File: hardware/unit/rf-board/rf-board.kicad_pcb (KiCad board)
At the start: 6 copper layers, 268 x 230 mm, 357 parts, among them J1 83-798 SO-239, J10 83-798 SO-239, J11 XT60PW-M, J12 XT60PW-M, J13 XT30PW-M, J14 Controller header, J2 83-798 SO-239, J3 83-798 SO-239, J4 SMA jack EXP, J5 SMA jack EXP, J6 SMA jack EXP, J7 83-798 SO-239, J8 83-798 SO-239, J9 83-798 SO-239, K101 RTD14012F, K102 RTD14012F, K103 RTD14012F, K104 RTD14012F, K105 RTD14012F, K106 RTD14012F, K107 RTD14012F, K108 RTD14012F, K109 RTD14012F, K110 RTD14012F, K111 RTD14012F, K201 RTD14012F, K202 RTD14012F, K203 RTD14012F, K204 RTD14012F, K205 RTD14012F, K206 RTD14012F, K207 RTD14012F, K208 RTD14012F, K209 RTD14012F, K210 RTD14012F, K211 RTD14012F, K301 RTD14012F, K302 RTD14012F, K303 RTD14012F, K304 RTD14012F, K305 RTD14012F, K306 RTD14012F, K307 RTD14012F, K308 RTD14012F, K309 RTD14012F, K310 RTD14012F, K311 RTD14012F, K401 RTD14012F, K501 RTD14012F, K601 RTD14012F, K701 RTD14012F, Q1 PMV50EPEA, Q101 BSS138BK, Q1011 BC857B, Q1012 IRFL9014, Q1013 BSS138BK, Q102 BSS138BK, Q1021 BC857B, Q1022 IRFL9014, Q1023 BSS138BK, Q103 BSS138BK, Q1031 BC857B, Q1032 IRFL9014, Q1033 BSS138BK, Q104 BSS138BK, Q1041 BC857B, Q1042 IRFL9014, Q1043 BSS138BK, Q105 BSS138BK, Q106 BSS138BK, Q107 BSS138BK, Q108 BSS138BK, Q109 BSS138BK, Q110 BSS138BK, Q111 BSS138BK, Q2 BSS138BK, Q201 BSS138BK, Q202 BSS138BK, Q203 BSS138BK, Q204 BSS138BK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

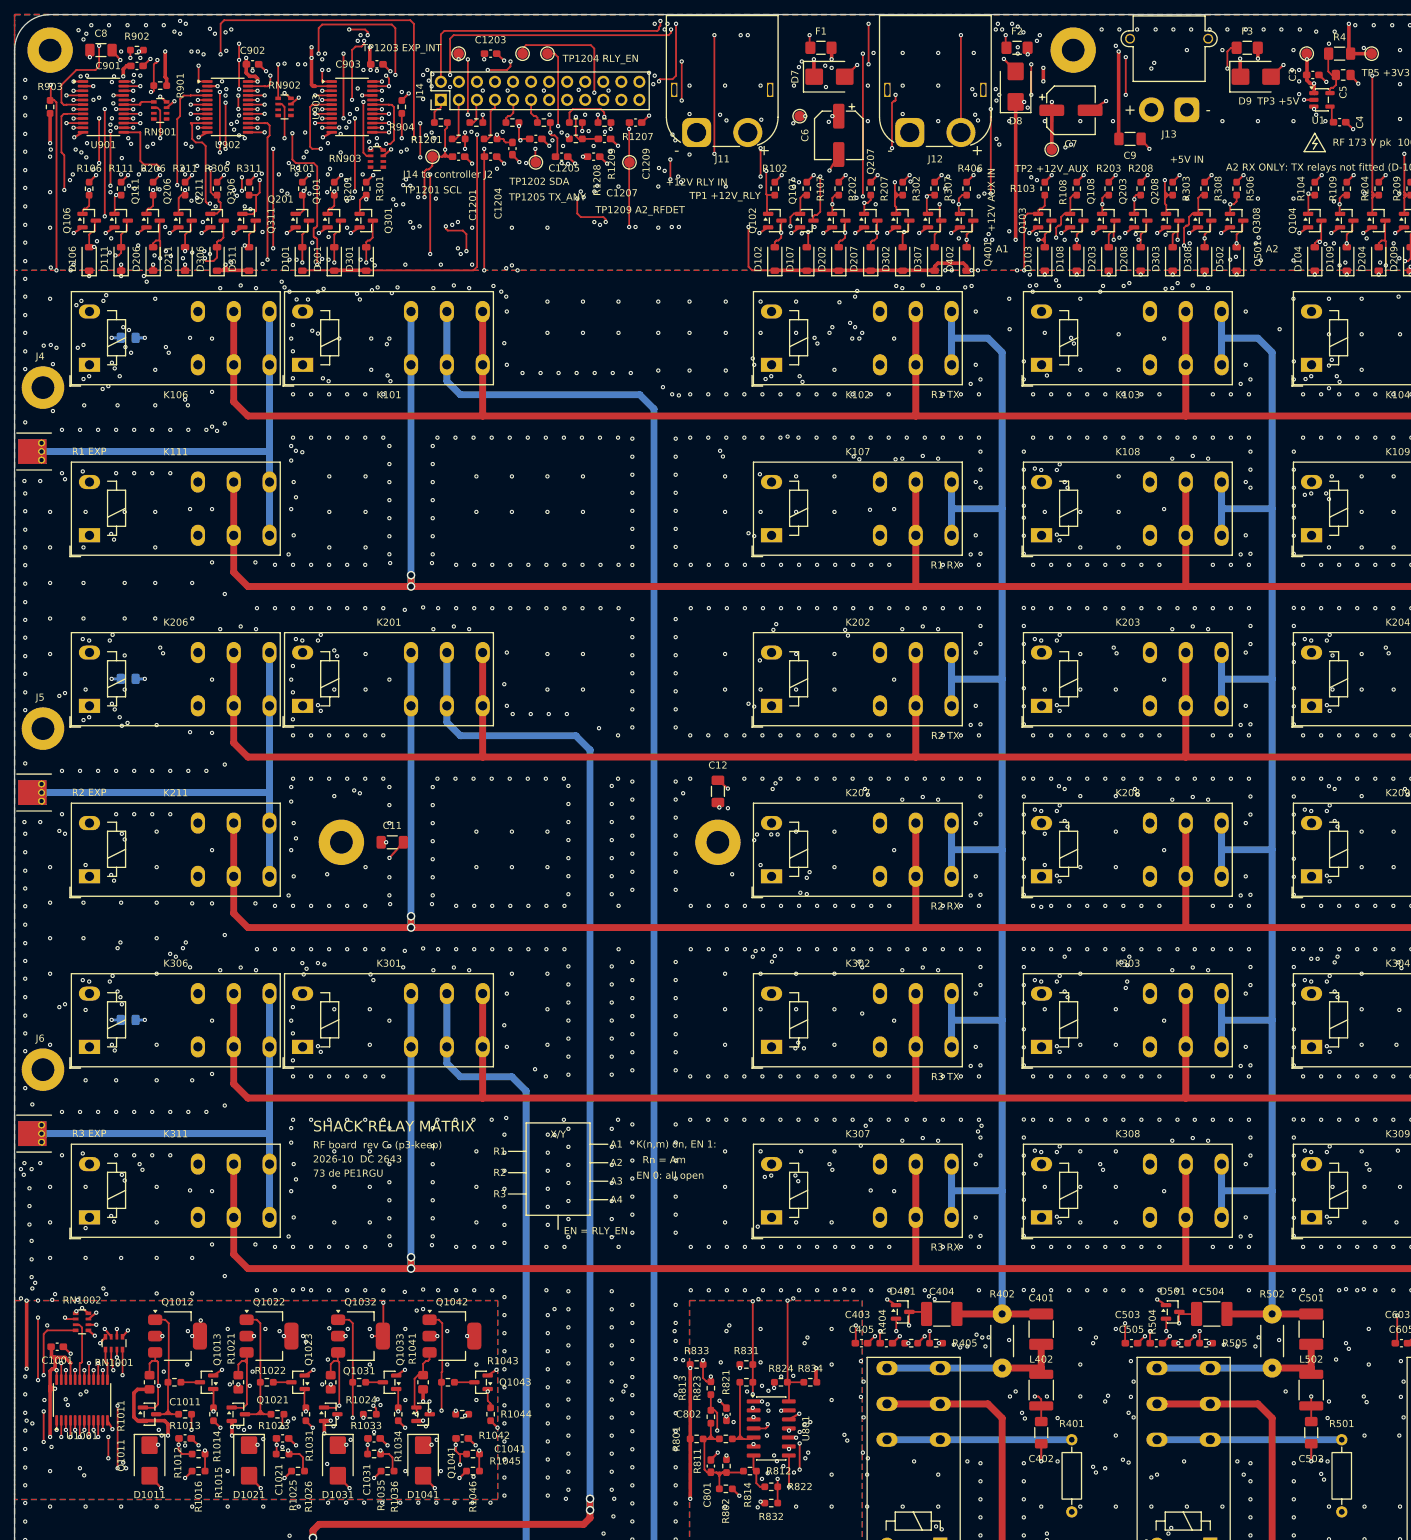
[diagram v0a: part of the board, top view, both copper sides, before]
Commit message: S-3: drain copper per bias-T FET on F.Cu and B.Cu
Each feed FET (Q1012/Q1022/Q1032/Q1042) gets an /A?_BIAS pour on F.Cu
around the tab and on B.Cu over its cell, with 9 thermal vias. About
415 mm2 (0.64 in2) per FET; estimated RthJA 70-75 K/W, Tj 110-114 C in a
held short at 55 C (C-17). stitch.py puts no grid vias in the cells.
RF layout p3-drain: 168/168 nets, 1124 vias, DRC 0 (30 pad-12 pairs as
before). D-193, M-111. Held-short test on the prototype to confirm.

Co-Authored-By: Claude Opus 5.5 <noreply@anthropic.com>
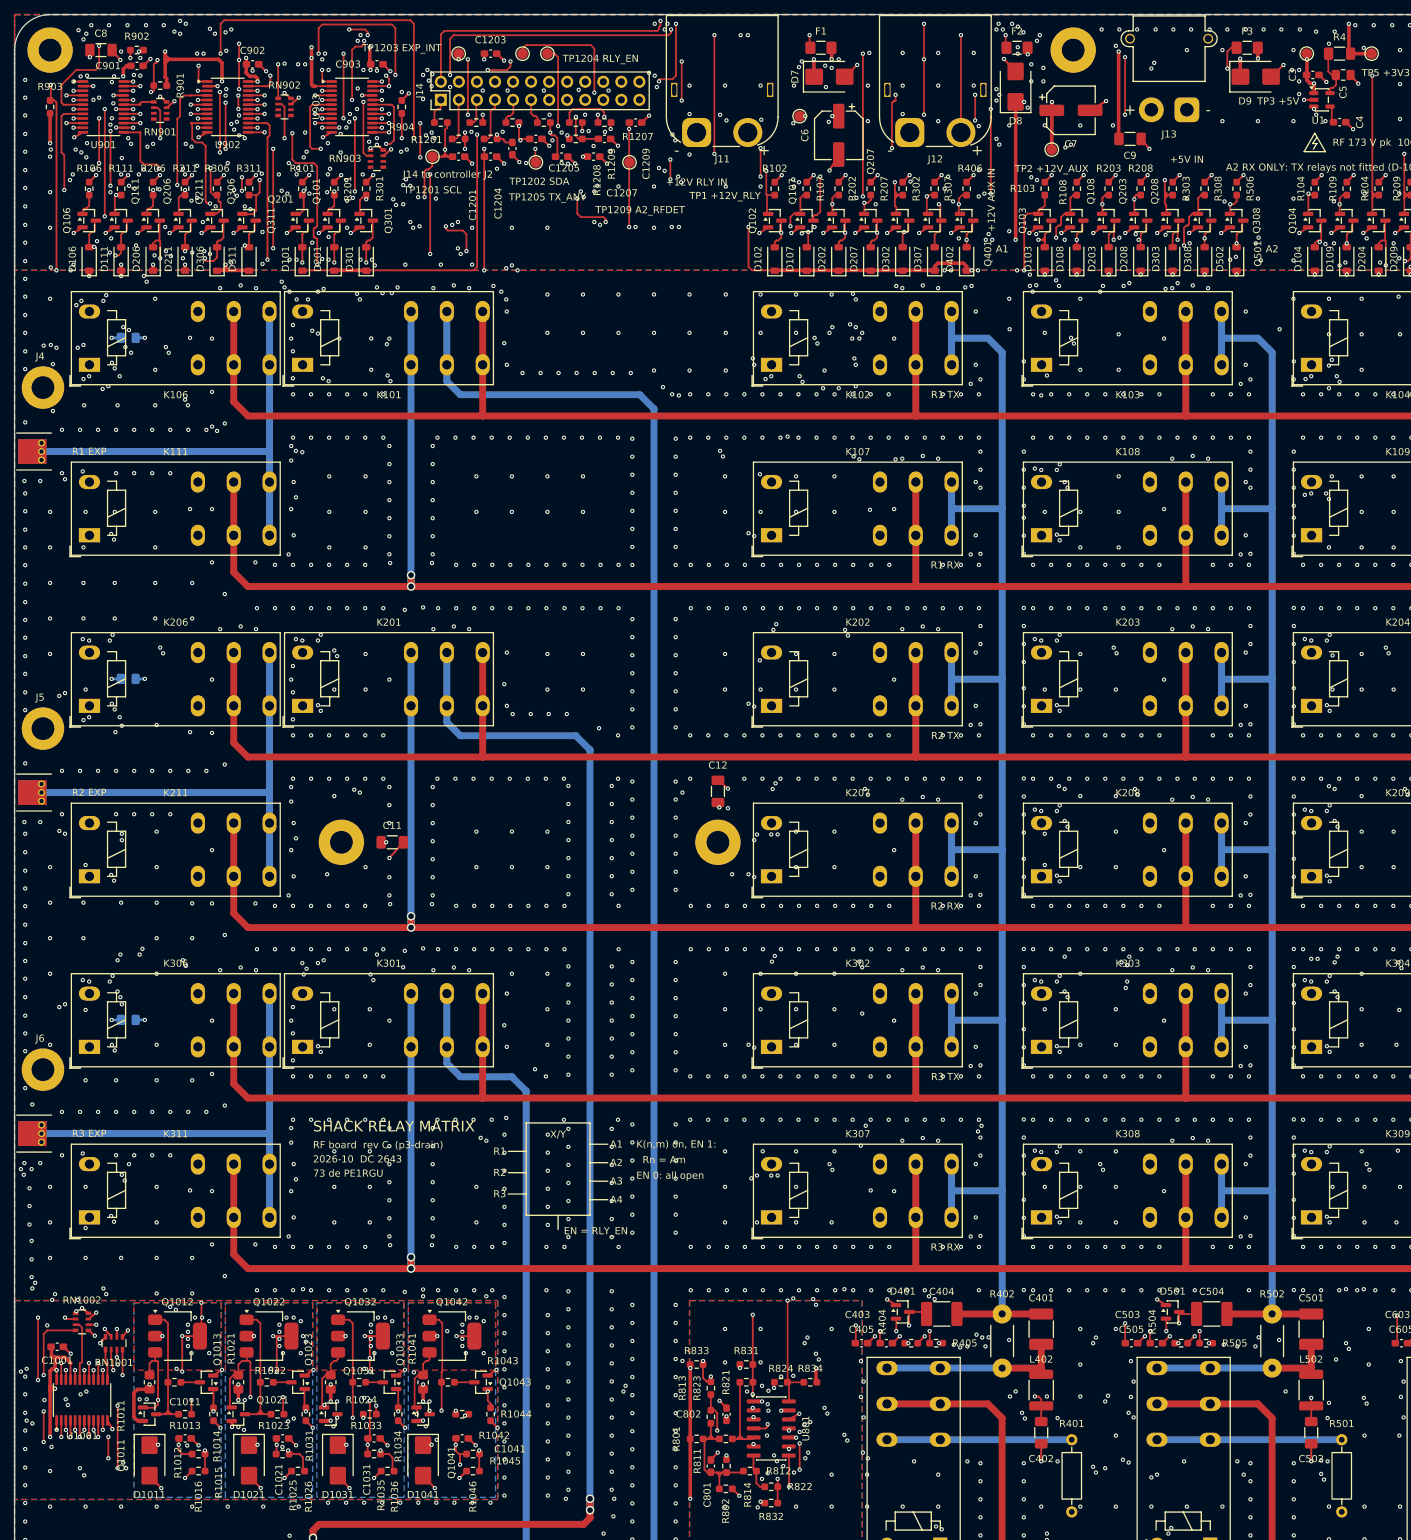
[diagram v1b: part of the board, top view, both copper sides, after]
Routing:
- net +5V: track 382.8 -> 404.9 mm, vias 18 -> 19
- net +12V_AUX: track 359.4 -> 349.5 mm, vias 19 -> 20
- net Net-(Q1011-B): track 25.7 -> 19.3 mm, vias 3 -> 2
- net Net-(Q1021-B): track 26.2 -> 22.4 mm, vias 3 -> 2
- net /A3_BIAS: track 236.7 -> 240.5 mm, vias 11 -> 24
- net /A1_BIAS: track 165.6 -> 168.1 mm, vias 8 -> 18
- net /A2_BIAS: track 216.3 -> 217.9 mm, vias 9 -> 19
- net +12V_SW: track 1160.4 -> 1161.3 mm
- net +3V3: track 643.3 -> 642.4 mm, vias 43 -> 41
- net Net-(D311-A): track 156.4 -> 155.7 mm
- net /IO expanders/A1_RFDET: track 270.5 -> 270.3 mm, vias 6 -> 5
- net /SCL: track 316.7 -> 316.6 mm, vias 19 -> 21
- net GND: vias 3298 -> 3275
- net /A4_BIAS: vias 15 -> 24
- added copper zone on B.Cu, net /A1_BIAS
- added copper zone on F.Cu, net /A1_BIAS
- added copper zone on B.Cu, net /A2_BIAS
- added copper zone on F.Cu, net /A2_BIAS
- added copper zone on B.Cu, net /A3_BIAS
- added copper zone on F.Cu, net /A3_BIAS
- added copper zone on B.Cu, net /A4_BIAS
- added copper zone on F.Cu, net /A4_BIAS
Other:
- board text added: "RF board rev C (p3-drain)"
- board text removed: "RF board rev C (p3-keep)"
